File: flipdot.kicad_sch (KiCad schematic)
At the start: 10 parts, among them J4 Conn_01x05_Pin, J8 Conn_01x05_Pin, Q1 FDN338P

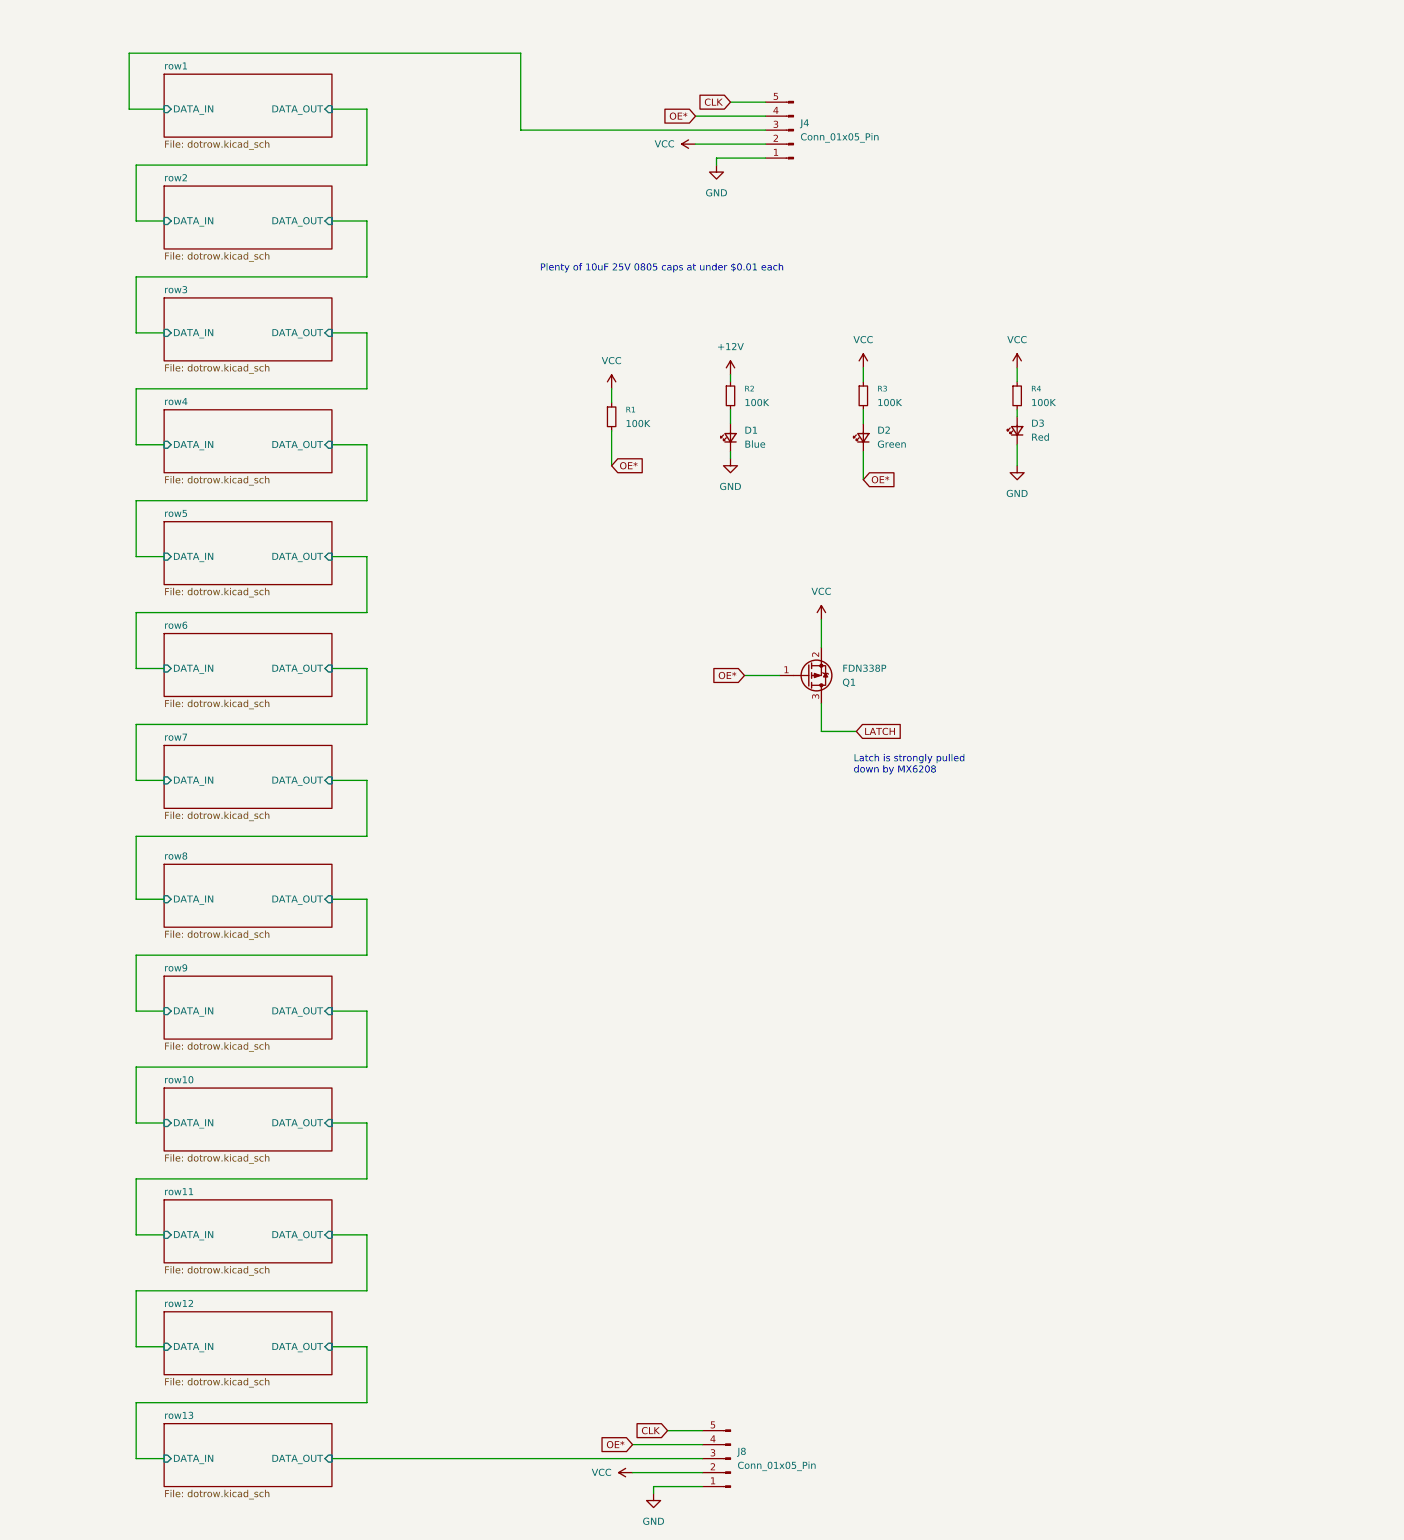
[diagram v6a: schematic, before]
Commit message: left/right test pads added
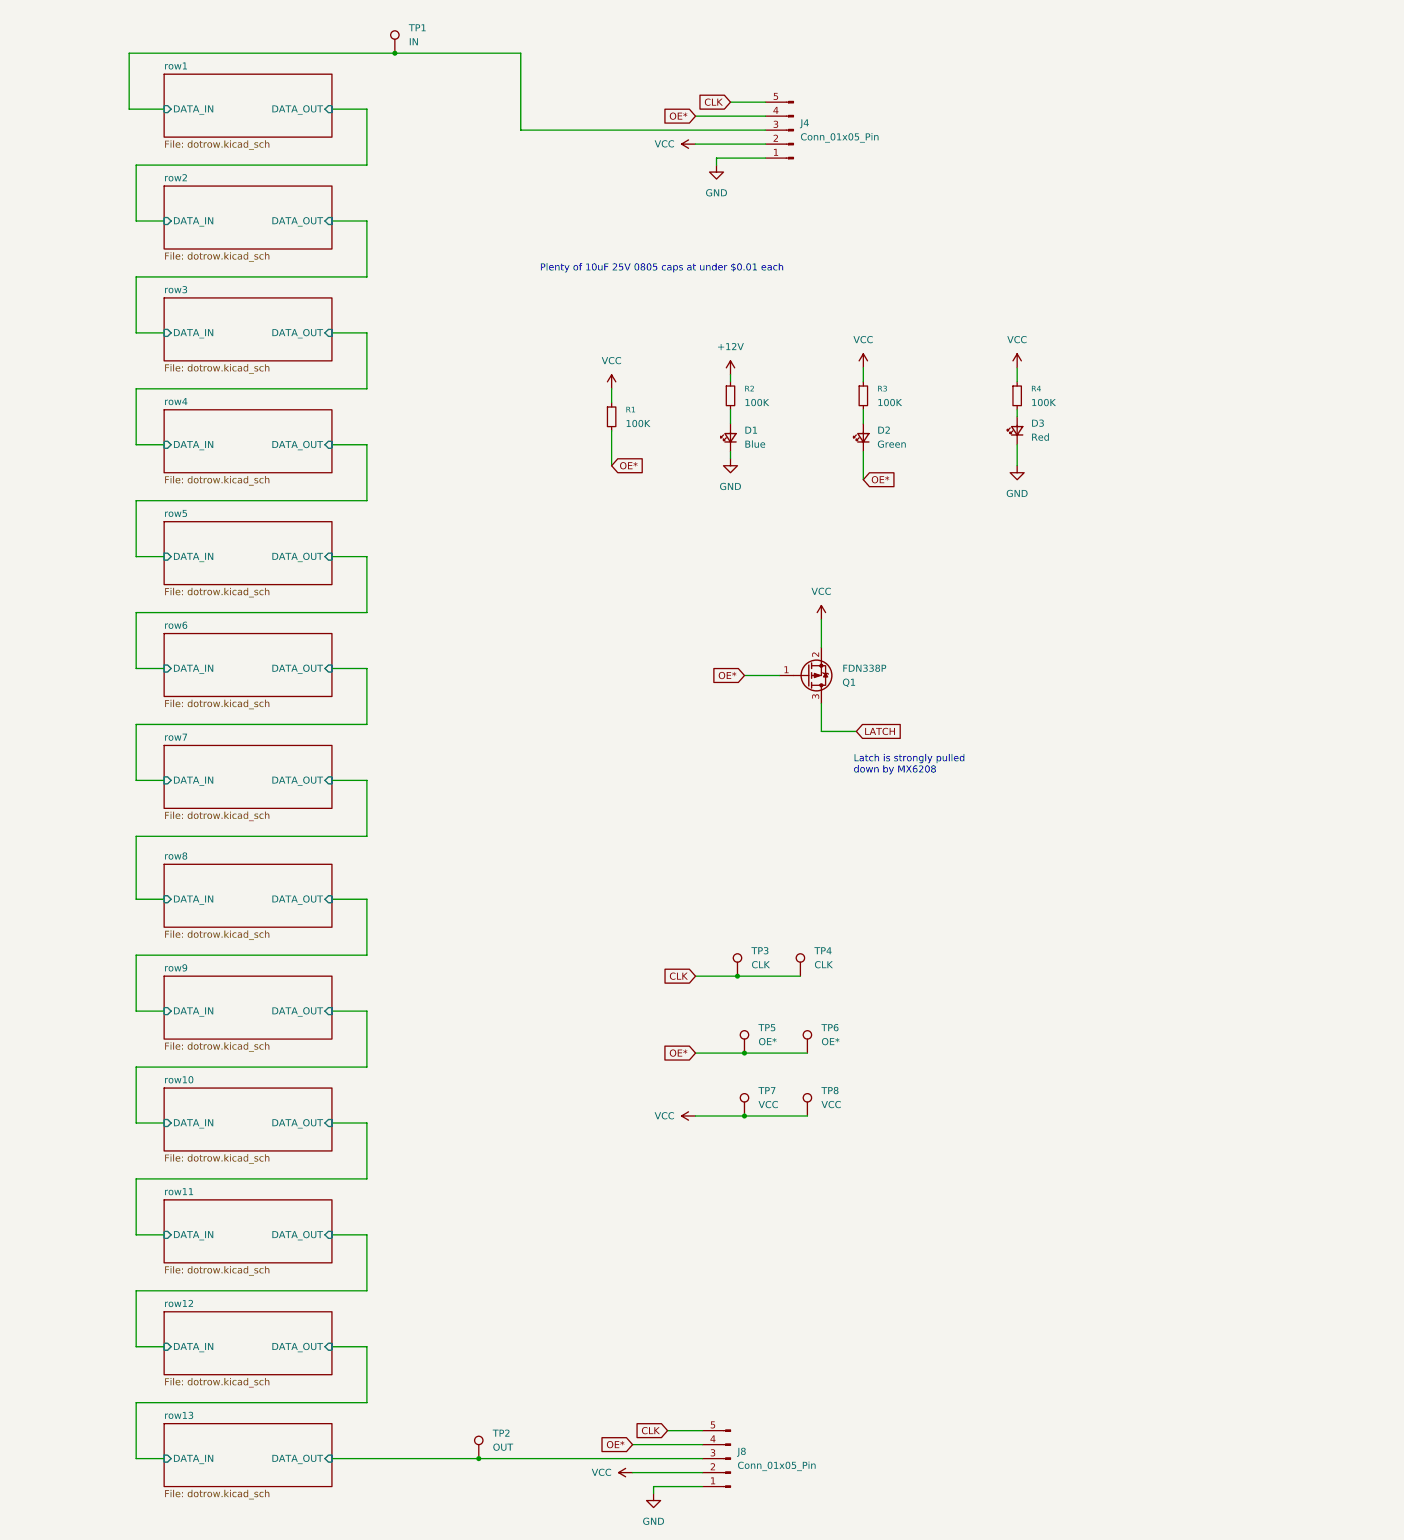
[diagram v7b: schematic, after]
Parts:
- added TP1: IN, TestPoint:TestPoint_Pad_D1.5mm, symbol Connector:TestPoint
- added TP2: OUT, TestPoint:TestPoint_Pad_D1.5mm, symbol Connector:TestPoint
- added TP3, TP4: CLK, TestPoint:TestPoint_Pad_D1.5mm, symbol Connector:TestPoint
- added TP5, TP6: OE*, TestPoint:TestPoint_Pad_D1.5mm, symbol Connector:TestPoint
- added TP7, TP8: VCC, TestPoint:TestPoint_Pad_D1.5mm, symbol Connector:TestPoint
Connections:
- net CLK: now also TP3.1, TP4.1
- net OE*: now also TP5.1, TP6.1
- net VCC: now also TP7.1, TP8.1
- net row1/DATA_IN: now also TP1.1
- net row13/DATA_OUT: now also TP2.1

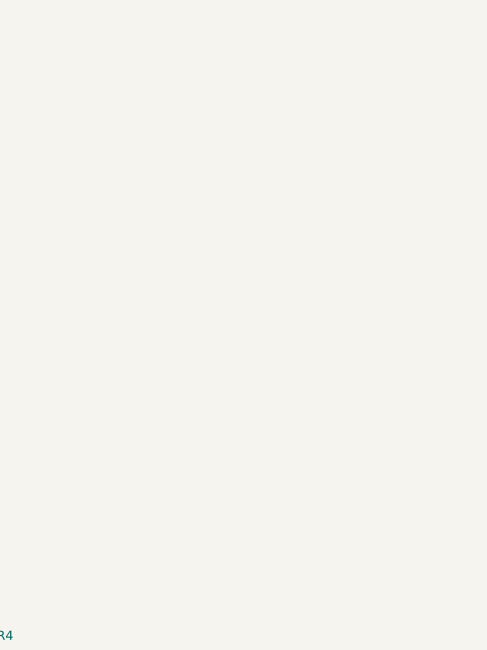
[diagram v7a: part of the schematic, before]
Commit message: add more electrolytics for 12v
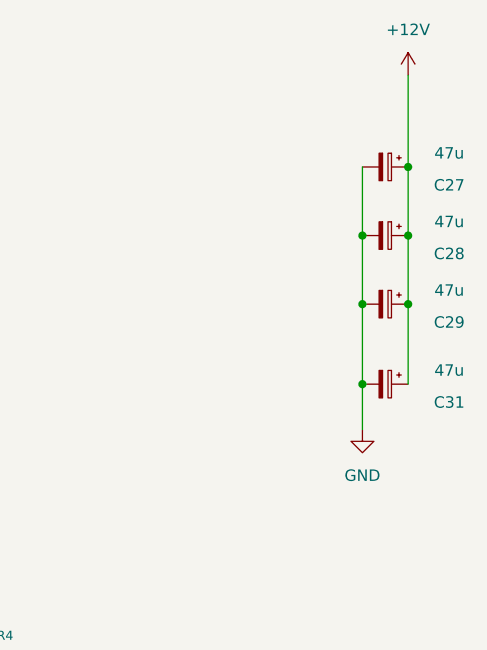
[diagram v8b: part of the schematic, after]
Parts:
- added C27, C28, C29, C31: 47u, Flipdot:CP_Elec_5x5.4_slim, symbol Device:C_Polarized_Small
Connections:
- net +12V: now also C27.1, C28.1, C29.1, C31.1
- net GND: now also C27.2, C28.2, C29.2, C31.2
